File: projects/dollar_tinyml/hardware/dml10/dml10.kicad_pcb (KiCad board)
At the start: 2 copper layers, 52 x 26 mm, 51 parts, among them J1 Conn_01x03, J2 USB_A, J3 Header 2.54mm, J4 Header 2.54mm, U1 CH32V003F4P6, U2 LTC4054ES5-4.2, U3 BM7161, U5 LIS3DH, U6 LMV358

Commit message: dollarml: Fixup headers
Board outline is only thing missing now?
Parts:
- removed BT1: Battery_Cell, Connector_PinHeader_2.54mm:PinHeader_1x02_P2.54mm_Vertical
- removed J3: Header 2.54mm, Connector_PinHeader_2.54mm:PinHeader_1x04_P2.54mm_Vertical
- added H1: MountingHole, dml10:Mousebite_0.6mmX8, F.Cu at (39.7, 44.5)
- added J6: Conn_01x03, Connector_PinHeader_1.27mm:PinHeader_1x03_P1.27mm_Vertical, F.Cu at (68.1, 41.2)
- J4: footprint Connector_PinHeader_2.54mm:PinHeader_1x06_P2.54mm_Vertical -> Connector_PinHeader_2.54mm:PinHeader_1x14_P2.54mm_Vertical
- U1: value CH32V003F4P6 -> PY32F003F16P6TU
- U2: value LTC4054ES5-4.2 -> LTC4054
- moved J4 21.7 mm to (43.2, 58.5)
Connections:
- J4 pad 1: VDD -> VBUS
- J4 pad 2: /SWDIO -> VDD
- J4 pad 3: /SWCLK -> GND
- J4 pad 4: /BOOT0 -> /SCL
- J4 pad 5: /RESET -> /SDA
- J4 pad 6: GND -> VDD
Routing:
- net VDD: track 101.7 -> 92.7 mm, vias 5 -> 6
- net VBUS: track 13.4 -> 21.5 mm, vias 0 -> 1
- net /LED_BLUE_N: track 12.5 -> 17.6 mm, vias 0 -> 1
- net /LED_BLUE_P: track 11.2 -> 15.6 mm
- net GND: track 57.8 -> 53.6 mm
- net /BOOT0: track 13.2 -> 9.44 mm, vias 1 -> 0
- net /SWDIO: track 9.90 -> 6.38 mm
- net /SWCLK: track 5.96 -> 9.26 mm, vias 0 -> 1
- net /RESET: track 19.1 -> 15.9 mm
- net /AUDIO_HIGH: track 18.0 -> 20.2 mm
- net /SDA: track 35.1 -> 34.2 mm
- net /SCL: track 30.5 -> 29.8 mm

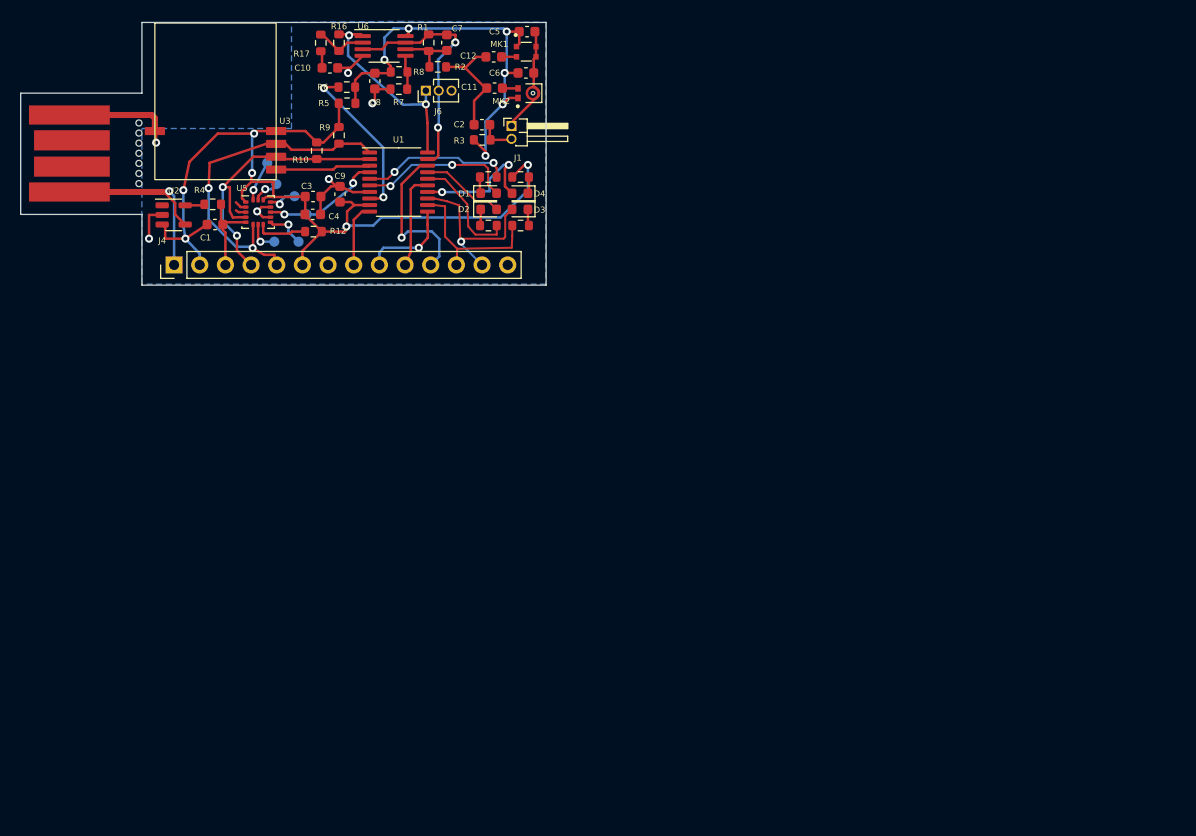
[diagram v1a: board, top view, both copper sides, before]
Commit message: dollarml: Fix proper PCB edge cuts
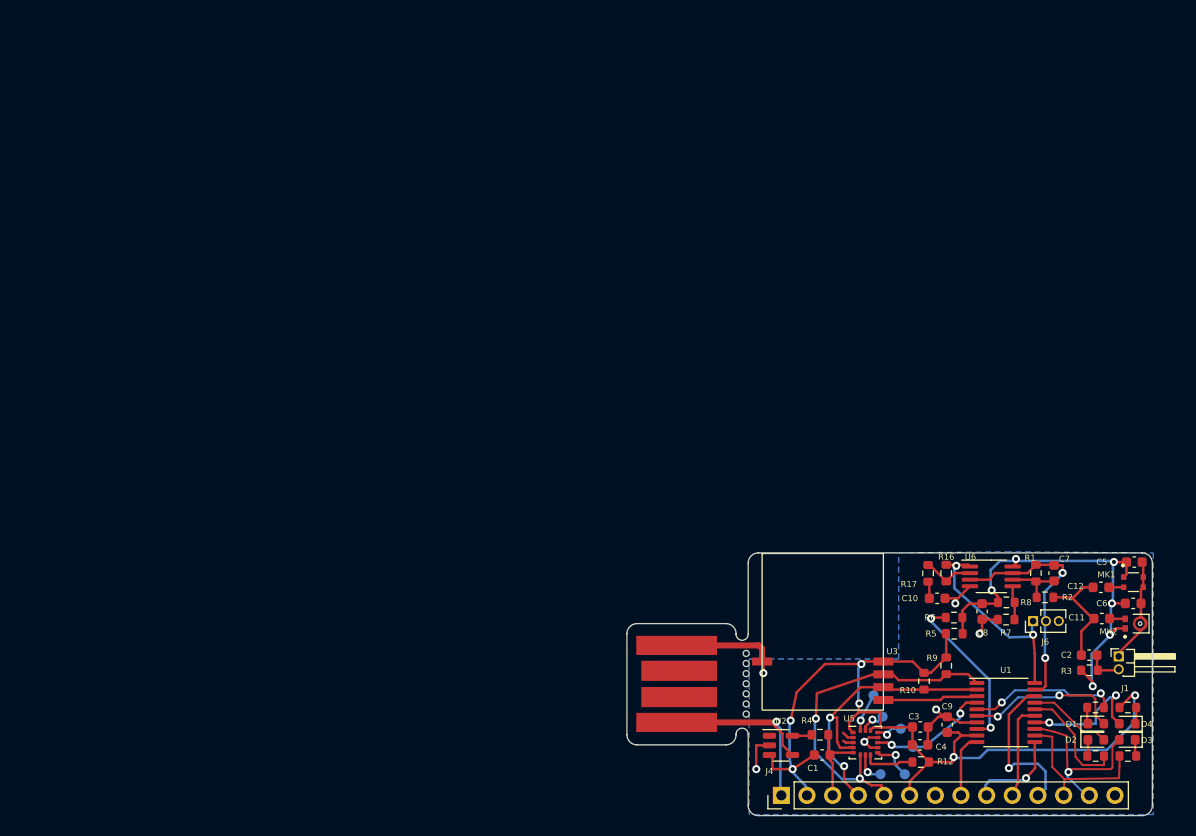
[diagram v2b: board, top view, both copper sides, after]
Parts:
- moved TP2 79.9 mm to (112.4, 101.1)
- moved TP3 79.9 mm to (113.3, 103.2)
- moved TP4 79.9 mm to (115.1, 104.4)
- moved TP5 79.9 mm to (116.3, 106.2)
- moved TP6 79.9 mm to (115.5, 108.9)
- moved TP7 79.9 mm to (113.1, 108.9)
- moved C11 79.8 mm to (135.0, 93.5)
- moved C12 79.8 mm to (134.9, 90.4)
- moved C2 79.8 mm to (133.8, 97.1)
- moved C3 79.8 mm to (117.0, 104.2)
- moved C5 79.8 mm to (138.2, 87.9)
- moved C6 79.8 mm to (138.1, 92.0)
- moved C7 79.8 mm to (130.3, 89.0)
- moved C8 79.8 mm to (123.2, 92.8)
- moved D1 79.8 mm to (134.4, 103.9)
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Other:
- outline, holes or cut-outs redrawn

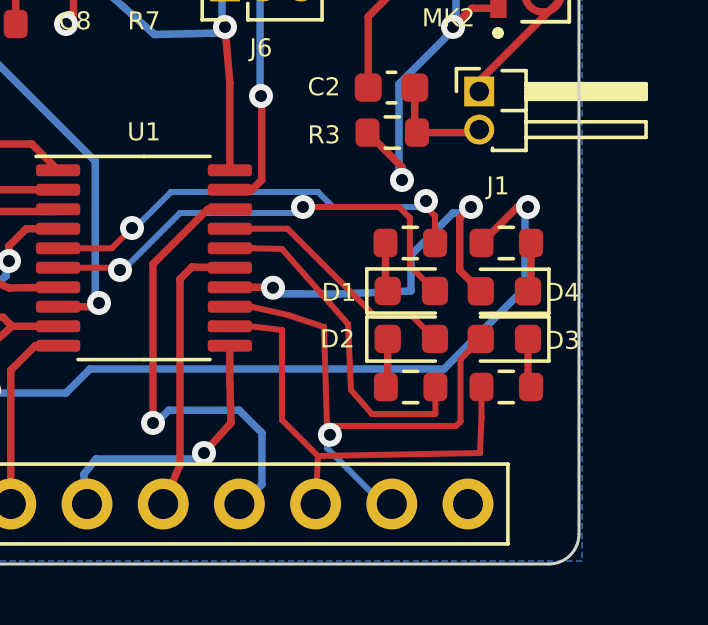
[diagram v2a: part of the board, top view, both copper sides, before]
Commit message: dollarml: Fixup BOM, submit to JLCPCB
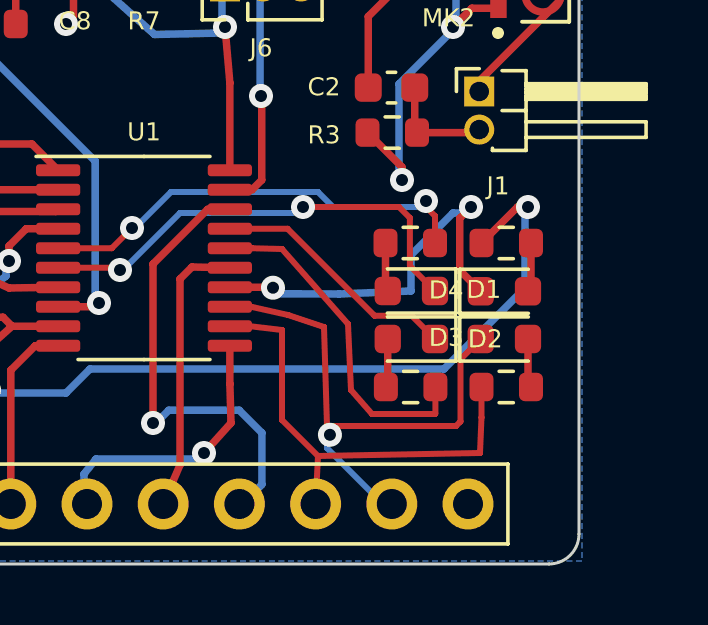
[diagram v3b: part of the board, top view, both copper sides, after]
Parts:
- C1: value C -> 10uF 10V
- C10, C11, C12, C2, C4, C8: value 10uF -> 10uF 10V
- C3: value 100nF -> 100nF 10V
- C5, C6, C9: value 10uF -> 1uF 10V
- C7: value 100pF -> 100pF 10V
- D1: value RED -> CLEAR RED
- D2: value GREEN -> CLEAR GREEN
- D3: value BLUE -> CLEAR BLUE
- D4: value WHITE -> CLEAR WHITE
- J1: value Conn_01x03 -> Header 2.54mm
- MK1: value IM73A135V01 -> LMA2718T421-OA5
- MK2: value IM73A135V01 -> LMA2718B381-OA5-2
- R11, R13: value R -> 120R
- R14, R15: value R -> 82R
- R3: value R -> 3k3
- R4: value R -> 10k
- R5: value R -> 0R
- R6: value 0ohm -> 0R
- U2: value LTC4054 -> LP4054HB5F
- U6: value LMV358 -> GS8632-MR
- turned D1 to 180 degrees
- turned D2 to 180 degrees
- turned D3 to 0 degrees
- turned D4 to 0 degrees
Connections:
- D1 pad 1: Net-(D1-K) -> /LED_RED_N
- D1 pad 2: /LED_RED_N -> Net-(D1-A)
- D2 pad 1: Net-(D2-K) -> /LED_GREEN_N
- D2 pad 2: /LED_GREEN_N -> Net-(D2-A)
- D3 pad 1: Net-(D3-K) -> /LED_BLUE_N
- D3 pad 2: /LED_BLUE_N -> Net-(D3-A)
- D4 pad 1: Net-(D4-K) -> /LED_WHITE_N
- D4 pad 2: /LED_WHITE_N -> Net-(D4-A)
- R11 pad 2: Net-(D1-K) -> Net-(D1-A)
- R13 pad 2: Net-(D2-K) -> Net-(D2-A)
- R14 pad 2: Net-(D3-K) -> Net-(D3-A)
- R15 pad 2: Net-(D4-K) -> Net-(D4-A)
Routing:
- net Net-(D4-K): track 1.65 -> 0.00 mm
- net Net-(D4-A): track 0.00 -> 1.65 mm
- net Net-(D3-K): track 1.64 -> 0.00 mm
- net Net-(D3-A): track 0.00 -> 1.64 mm
- net Net-(D1-K): track 1.63 -> 0.00 mm
- net Net-(D1-A): track 0.00 -> 1.63 mm
- net Net-(D2-K): track 1.63 -> 0.00 mm
- net Net-(D2-A): track 0.00 -> 1.63 mm
